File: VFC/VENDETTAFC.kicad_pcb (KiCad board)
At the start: 6 copper layers, 40 x 40 mm, 74 parts, among them IC1 MP1584EN-LF-Z, IC2 MP1584EN-LF-Z, J1 Conn_01x08_Socket, J2 Conn_01x06_Socket, J3 Conn_01x06_Socket, J4 Conn_01x03_Socket, P1 USB_C_Plug_USB2.0, SW1 SW_Push, U1 STM32F722RETx, U2 ICM-20948, U3 RT9701, U4 USBLC6-2P6, U5 W25Q128JVS, Y1 Crystal

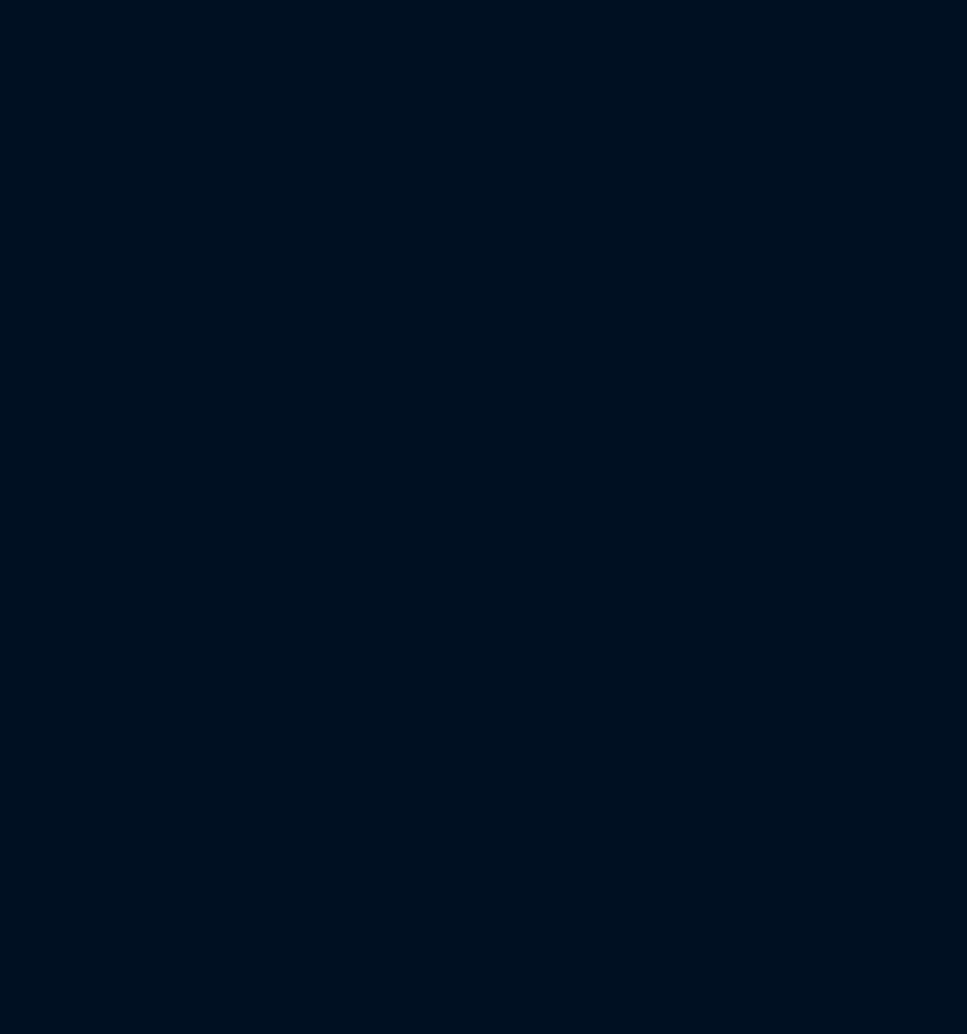
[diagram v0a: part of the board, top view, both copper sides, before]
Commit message: Updated VFC schematic
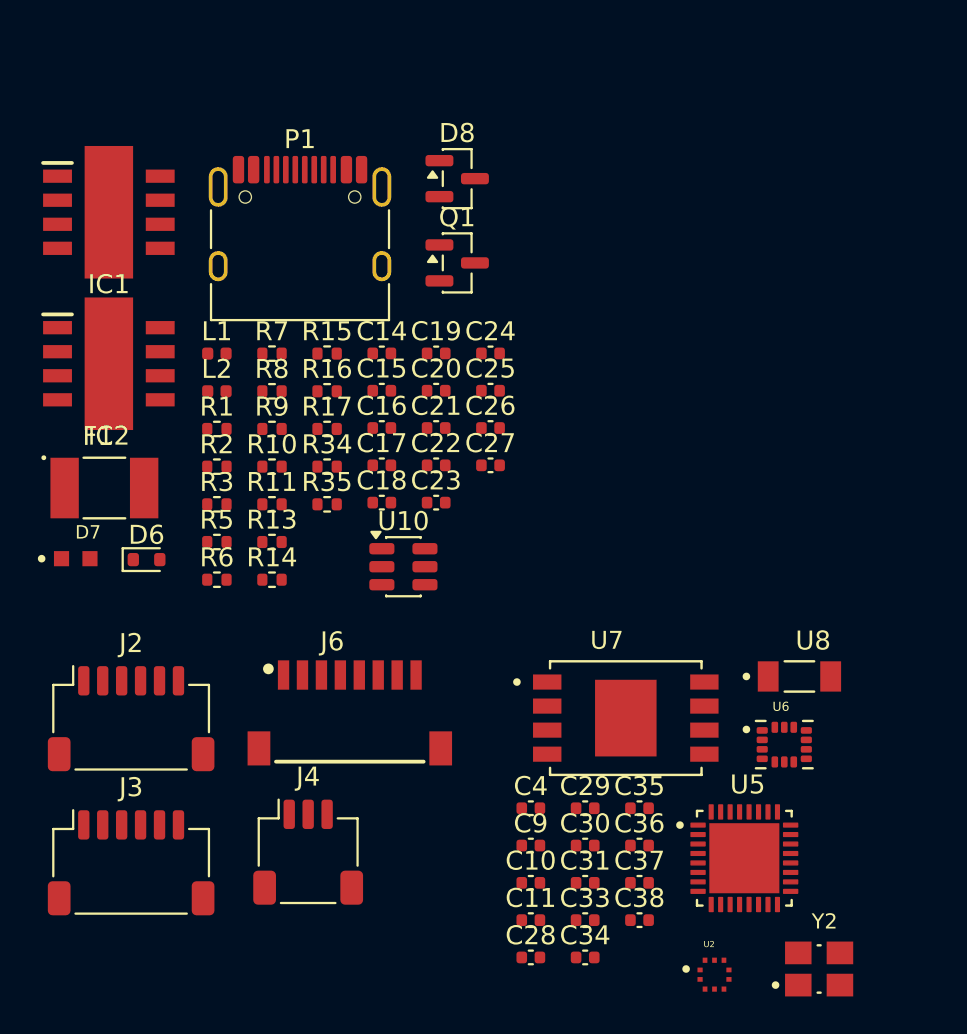
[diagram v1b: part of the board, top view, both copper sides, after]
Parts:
- added C10: 10nF, Capacitor_SMD:C_0402_1005Metric, F.Cu at (122.6, 145.5)
- added C11: 100nF, Capacitor_SMD:C_0402_1005Metric, F.Cu at (122.6, 147.5)
- added C14: 100nF, Capacitor_SMD:C_0402_1005Metric, F.Cu at (114.8, 117.6)
- added C15: 100nF, Capacitor_SMD:C_0402_1005Metric, F.Cu at (114.8, 119.5)
- added C16: 10uF, Capacitor_SMD:C_0402_1005Metric, F.Cu at (114.8, 121.5)
- added C17: 10uF, Capacitor_SMD:C_0402_1005Metric, F.Cu at (114.8, 123.5)
- added C18: 1uF, Capacitor_SMD:C_0402_1005Metric, F.Cu at (114.8, 125.4)
- added C19: 220pF, Capacitor_SMD:C_0402_1005Metric, F.Cu at (117.6, 117.6)
- added C20: 22uF, Capacitor_SMD:C_0402_1005Metric, F.Cu at (117.6, 119.5)
- added C21: 22uF, Capacitor_SMD:C_0402_1005Metric, F.Cu at (117.6, 121.5)
- added C22: 10uF, Capacitor_SMD:C_0402_1005Metric, F.Cu at (117.6, 123.5)
- added C23: 10uF, Capacitor_SMD:C_0402_1005Metric, F.Cu at (117.6, 125.4)
- added C24: 1uF, Capacitor_SMD:C_0402_1005Metric, F.Cu at (120.5, 117.6)
- added C25: 220pF, Capacitor_SMD:C_0402_1005Metric, F.Cu at (120.5, 119.5)
- added C26: 22uF, Capacitor_SMD:C_0402_1005Metric, F.Cu at (120.5, 121.5)
- added C27: 22uF, Capacitor_SMD:C_0402_1005Metric, F.Cu at (120.5, 123.5)
- added C28: 100nF, Capacitor_SMD:C_0402_1005Metric, F.Cu at (122.6, 149.5)
- added C29: 0.1uF, Capacitor_SMD:C_0402_1005Metric, F.Cu at (125.5, 141.6)
- added C30: 1pF, Capacitor_SMD:C_0402_1005Metric, F.Cu at (125.5, 143.5)
- added C31: 1pF, Capacitor_SMD:C_0402_1005Metric, F.Cu at (125.5, 145.5)
- added C33: 10nF, Capacitor_SMD:C_0402_1005Metric, F.Cu at (125.5, 147.5)
- added C34: 1uF, Capacitor_SMD:C_0402_1005Metric, F.Cu at (125.5, 149.5)
- added C35: 0.1uF, Capacitor_SMD:C_0402_1005Metric, F.Cu at (128.4, 141.6)
- added C36: 0.1uF, Capacitor_SMD:C_0402_1005Metric, F.Cu at (128.4, 143.5)
- added C37: 10uF, Capacitor_SMD:C_0402_1005Metric, F.Cu at (128.4, 145.5)
- added C38: 100nF, Capacitor_SMD:C_0402_1005Metric, F.Cu at (128.4, 147.5)
- added C4: 0.1uF, Capacitor_SMD:C_0402_1005Metric, F.Cu at (122.6, 141.6)
- added C9: 2.2uF, Capacitor_SMD:C_0402_1005Metric, F.Cu at (122.6, 143.5)
- added D6: LTVS16H5, Diode_SMD:D_SOD-523, F.Cu at (102.3, 128.4)
- added D7: KT-0603R, KT-0603R:LED_KT-0603R, F.Cu at (98.6, 128.4)
- added D8: BAT54C, Package_TO_SOT_SMD:SOT-23, F.Cu at (118.7, 108.3)
- added F1: MF-MSMF050-2, MF-MSMF050-2:FUSM4632X85, F.Cu at (100.1, 124.7)
- added IC1: MP1584EN-LF-Z, MP1584EN-LF-Z:SOIC127P600X170-9N, F.Cu at (100.3, 110.1)
- added IC2: MP1584EN-LF-Z, MP1584EN-LF-Z:SOIC127P600X170-9N, F.Cu at (100.3, 118.1)
- added J2: Conn_01x06_Socket, Connector_JST:JST_SH_SM06B-SRSS-TB_1x06-1MP_P1.00mm_Horizontal, F.Cu at (101.5, 136.8)
- added J3: Conn_01x06_Socket, Connector_JST:JST_SH_SM06B-SRSS-TB_1x06-1MP_P1.00mm_Horizontal, F.Cu at (101.5, 144.5)
- added J4: Conn_01x03_Socket, Connector_JST:JST_SH_SM03B-SRSS-TB_1x03-1MP_P1.00mm_Horizontal, F.Cu at (110.9, 143.9)
- added J6: SM08B-SRSS-TB_LF__SN_, SM08B-SRSS-TB_LF__SN_:JST_SM08B-SRSS-TB_LF__SN_, F.Cu at (113.1, 139.3)
- added L1: 10uH, Inductor_SMD:L_0402_1005Metric, F.Cu at (106.1, 117.6)
- added L2: 10uH, Inductor_SMD:L_0402_1005Metric, F.Cu at (106.1, 119.6)
- added P1: USB_C_Plug_USB2.0, Connector_USB:USB_C_Receptacle_HRO_TYPE-C-31-M-12, F.Cu at (110.4, 111.9)
- added Q1: AO3400A, Package_TO_SOT_SMD:SOT-23, F.Cu at (118.7, 112.8)
- added R1: 5k1, Resistor_SMD:R_0402_1005Metric, F.Cu at (106.1, 121.5)
- added R10: 20, Resistor_SMD:R_0402_1005Metric, F.Cu at (109.0, 123.5)
- added R11: 68K1, Resistor_SMD:R_0402_1005Metric, F.Cu at (109.0, 125.5)
- added R13: 200K, Resistor_SMD:R_0402_1005Metric, F.Cu at (109.0, 127.5)
- added R14: 20, Resistor_SMD:R_0402_1005Metric, F.Cu at (109.0, 129.5)
- added R15: 51K, Resistor_SMD:R_0402_1005Metric, F.Cu at (111.9, 117.6)
- added R16: 7K5, Resistor_SMD:R_0402_1005Metric, F.Cu at (111.9, 119.6)
- added R17: 41K2, Resistor_SMD:R_0402_1005Metric, F.Cu at (111.9, 121.5)
- added R2: 80, Resistor_SMD:R_0402_1005Metric, F.Cu at (106.1, 123.5)
- added R3: 80, Resistor_SMD:R_0402_1005Metric, F.Cu at (106.1, 125.5)
- added R34: 1K, Resistor_SMD:R_0402_1005Metric, F.Cu at (111.9, 123.5)
- added R35: 10K, Resistor_SMD:R_0402_1005Metric, F.Cu at (111.9, 125.5)
- added R5: 68K1, Resistor_SMD:R_0402_1005Metric, F.Cu at (106.1, 127.5)
- added R6: 200K, Resistor_SMD:R_0402_1005Metric, F.Cu at (106.1, 129.5)
- added R7: 51K, Resistor_SMD:R_0402_1005Metric, F.Cu at (109.0, 117.6)
- added R8: 41K2, Resistor_SMD:R_0402_1005Metric, F.Cu at (109.0, 119.6)
- added R9: 3K92, Resistor_SMD:R_0402_1005Metric, F.Cu at (109.0, 121.5)
- added U10: USBLC6-2SC6, Package_TO_SOT_SMD:SOT-23-6, F.Cu at (115.9, 128.8)
- added U2: BMP388, BMP388:XDCR_BMP388, F.Cu at (132.3, 150.4)
- added U5: ESP32-C3, ESP32-C3:QFN50P500X500X90-33N, F.Cu at (133.9, 144.2)
- added U6: ICM-42688-P, ICM-42688-P:PQFN50P300X250X97-14N, F.Cu at (136.0, 138.2)
- added U7: W25N04KVZEIR, W25N04KVZEIR:IC_W25N04KVZEIR, F.Cu at (127.7, 136.8)
- added U8: ~, crossair-ca-c03-antenna-1.snapshot.1:CA-C03, F.Cu at (136.8, 134.6)
- added Y2: C3E-40.000-10-1015-X-R, C3E-40.000-10-1015-X-R:XTAL_C3E-40.000-10-1015-X-R, F.Cu at (137.9, 150.1)
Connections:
- C1 pad 1: +3.3V -> ESP_EN
- C13 pad 1: +3.3V -> ESP_EN
- C2 pad 1: +3.3V -> ESP_EN
- C3 pad 1: +3.3V -> ESP_EN
- C5 pad 1: +3.3V -> ESP_EN
- C6 pad 1: +3.3V -> ESP_EN
- C7 pad 1: +3.3V -> ESP_EN
- D1 pad 2: +3.3V -> ESP_EN
- SW1 pad 1: +3.3V -> ESP_EN
- U1 pad 1: +3.3V -> ESP_EN
- U1 pad 13: +3.3V -> ESP_EN
- U1 pad 19: +3.3V -> ESP_EN
- U1 pad 32: +3.3V -> ESP_EN
- U1 pad 48: +3.3V -> ESP_EN
- U1 pad 64: +3.3V -> ESP_EN
- U3 pad 1: +3.3V -> ESP_EN
- U3 pad 5: +3.3V -> ESP_EN
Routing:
- net ESP_EN: track 0.00 -> 28.1 mm, vias 0 -> 10
- net +3.3V: track 36.7 -> 8.62 mm, vias 12 -> 2
- added copper zone on B.Cu, net ESP_EN
- added copper zone on In4.Cu, net ESP_EN
- removed copper zone on B.Cu, net +3.3V
- removed copper zone on In4.Cu, net +3.3V

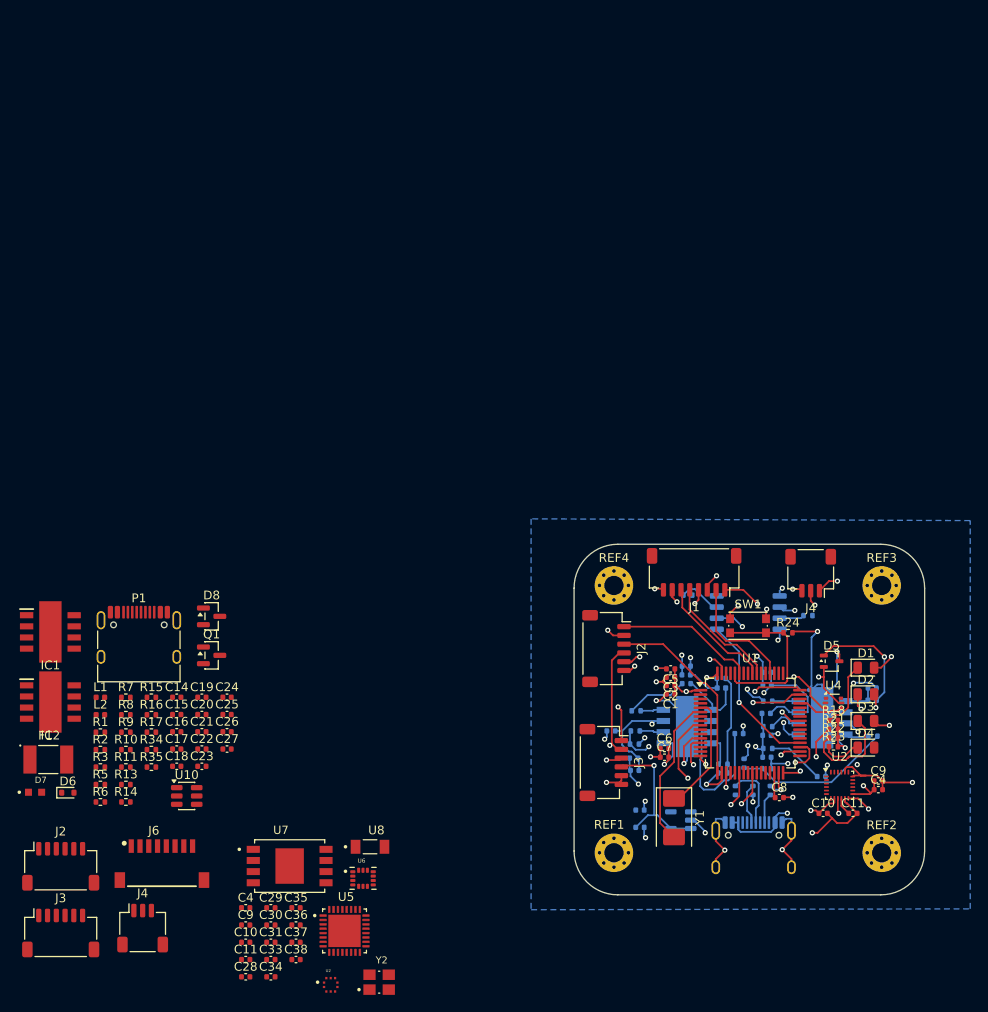
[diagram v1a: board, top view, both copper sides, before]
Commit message: VFC PCB components placements complete
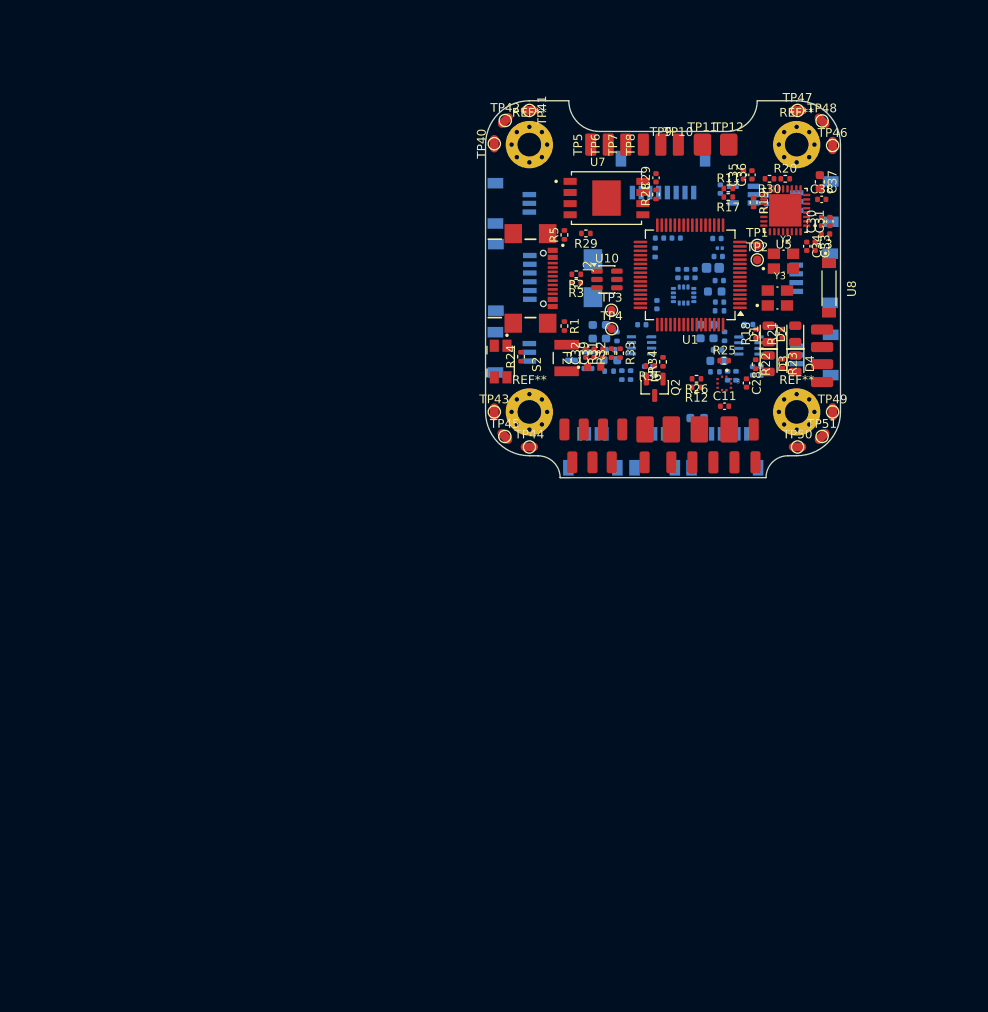
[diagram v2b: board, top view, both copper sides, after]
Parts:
- removed the C10 at (122.6, 145.5)
- removed the C10 at (188.5, 130.8)
- removed the C11 at (122.6, 147.5)
- removed the C11 at (191.9, 130.8)
- removed the C14 at (114.8, 117.6)
- removed the C14 at (172.9, 116.0)
- removed the C15 at (114.8, 119.5)
- removed the C15 at (194.1, 116.5)
- removed the C16 at (114.8, 121.5)
- removed the C16 at (167.0, 125.9)
- removed the C17 at (114.8, 123.5)
- removed the C17 at (164.3, 121.4)
- removed the C18 at (114.8, 125.4)
- removed the C18 at (166.9, 124.5)
- removed the C19 at (117.6, 117.6)
- removed the C19 at (178.9, 121.7)
- removed the C20 at (117.6, 119.5)
- removed the C20 at (172.9, 114.0)
- removed the C21 at (117.6, 121.5)
- removed the C21 at (172.9, 115.0)
- removed the C22 at (117.6, 123.5)
- removed the C22 at (182.0, 119.4)
- removed the C23 at (117.6, 125.4)
- removed the C23 at (182.1, 116.2)
- removed C24 (x2): 1uF, Capacitor_SMD:C_0402_1005Metric
- removed C25 (x2): 220pF, Capacitor_SMD:C_0402_1005Metric
- removed C26 (x2), C27 (x2): 22uF, Capacitor_SMD:C_0402_1005Metric
- removed the C4 at (194.8, 128.1)
- removed the C4 at (122.6, 141.6)
- removed the C9 at (194.8, 127.1)
- removed the C9 at (122.6, 143.5)
- removed D6: LTVS16H5, Diode_SMD:D_SOD-523
- removed F1: MF-MSMF050-2, MF-MSMF050-2:FUSM4632X85
- removed IC1 (x2), IC2 (x2): MP1584EN-LF-Z, MP1584EN-LF-Z:SOIC127P600X170-9N
- removed the J2 at (163.8, 112.0)
- removed the J2 at (101.5, 136.8)
- removed the J3 at (163.5, 125.0)
- removed the J3 at (101.5, 144.5)
- removed J4 (x2): Conn_01x03_Socket, Connector_JST:JST_SH_SM03B-SRSS-TB_1x03-1MP_P1.00mm_Horizontal
- removed the L1 at (106.1, 117.6)
- removed the L1 at (176.9, 116.5)
- removed the L2 at (106.1, 119.6)
- removed the L2 at (194.1, 117.9)
- removed P1 (x2): USB_C_Plug_USB2.0, Connector_USB:USB_C_Receptacle_HRO_TYPE-C-31-M-12
- removed Q1: AO3400A, Package_TO_SOT_SMD:SOT-23
- removed the R1 at (106.1, 121.5)
- removed the R1 at (182.5, 128.2)
- removed the R10 at (109.0, 123.5)
- removed the R10 at (167.2, 119.1)
- removed the R11 at (109.0, 125.5)
- removed the R11 at (182.2, 123.4)
- removed the R13 at (109.0, 127.5)
- removed the R13 at (182.2, 120.9)
- removed the R14 at (109.0, 129.5)
- removed the R14 at (182.2, 118.0)
- removed the R15 at (111.9, 117.6)
- removed the R15 at (194.2, 122.0)
- removed the R16 at (111.9, 119.6)
- removed the R16 at (179.5, 125.1)
- removed the R17 at (111.9, 121.5)
- removed the R17 at (182.1, 125.7)
- removed the R2 at (106.1, 123.5)
- removed the R2 at (180.5, 128.2)
- removed the R3 at (106.1, 125.5)
- removed the R3 at (178.5, 128.2)
- removed the R5 at (106.1, 127.5)
- removed the R5 at (167.0, 122.9)
- removed R6 (x2): 200K, Resistor_SMD:R_0402_1005Metric
- removed the R7 at (109.0, 117.6)
- removed the R7 at (177.1, 125.2)
- removed the R8 at (109.0, 119.6)
- removed the R8 at (176.9, 115.4)
- removed the R9 at (109.0, 121.5)
- removed the R9 at (177.1, 126.2)
- removed REF1, REF2, REF3, REF4: MountingHole_2.2mm_M2_Pad_Via, MountingHole:MountingHole_2.2mm_M2_Pad_Via
- removed SW1: SW_Push, Button_Switch_SMD:SW_Push_1P1T_NO_CK_KMR2
- removed the U2 at (190.4, 127.6)
- removed the U2 at (132.3, 150.4)
- removed the U5 at (133.9, 144.2)
- removed the U5 at (180.0, 107.9)
- removed Y1: Crystal, Crystal:Crystal_SMD_0603-2Pin_6.0x3.5mm
- added C10: 10nF, Capacitor_SMD:C_0402_1005Metric, B.Cu at (171.9, 69.2)
- added C11: 100nF, Capacitor_SMD:C_0402_1005Metric, F.Cu at (177.3, 84.3)
- added C14: 100nF, Capacitor_SMD:C_0402_1005Metric, B.Cu at (180.5, 80.3)
- added C15: 100nF, Capacitor_SMD:C_0402_1005Metric, B.Cu at (168.2, 80.3)
- added C16: 100nF, Capacitor_SMD:C_0402_1005Metric, B.Cu at (176.7, 70.0)
- added C17: 22uF, Capacitor_SMD:C_0603_1608Metric, B.Cu at (176.0, 75.8)
- added C18: 100uF, Capacitor_SMD:C_0603_1608Metric, B.Cu at (174.5, 75.8)
- added C19: 22uF, Capacitor_SMD:C_0603_1608Metric, B.Cu at (163.8, 75.8)
- added C20: 47uF, Capacitor_SMD:C_0603_1608Metric, B.Cu at (176.4, 79.2)
- added C21: 100uF, Capacitor_SMD:C_0603_1608Metric, B.Cu at (162.2, 75.8)
- added C22: 47uF, Capacitor_SMD:C_0603_1608Metric, B.Cu at (164.2, 79.1)
- added C23: 100nF, Capacitor_SMD:C_0402_1005Metric, B.Cu at (169.6, 72.8)
- added C32: 100nF, Capacitor_SMD:C_0402_1005Metric, F.Cu at (161.4, 78.3)
- added C39: 1uF, Capacitor_SMD:C_0402_1005Metric, F.Cu at (162.4, 78.3)
- added C4: 0.1uF, Capacitor_SMD:C_0402_1005Metric, B.Cu at (173.9, 69.2)
- added C40: 100uF, Capacitor_SMD:C_0603_1608Metric, B.Cu at (174.2, 85.7)
- added C41: 0.1uF, Capacitor_SMD:C_0402_1005Metric, B.Cu at (180.0, 75.0)
- added C42: 0.1uF, Capacitor_SMD:C_0402_1005Metric, B.Cu at (167.8, 75.0)
- added C9: 2.2uF, Capacitor_SMD:C_0402_1005Metric, B.Cu at (172.9, 69.2)
- added F2: MICROASMD010F-2, MICROASMD010F-2:FUSE_MICROASMD010F_LTF, F.Cu at (159.2, 78.8)
- added FL1: 120, BLM03EB500SZ1D:BEADC0603X33N, B.Cu at (176.7, 66.3)
- added J10: SM04B-SRSS-TB_LF__SN_, SM04B-SRSS-TB_LF__SN_:JST_SM04B-SRSS-TB_LF__SN_, B.Cu at (185.4, 69.8)
- added J11: SM04B-SRSS-TB_LF__SN_, SM04B-SRSS-TB_LF__SN_:JST_SM04B-SRSS-TB_LF__SN_, B.Cu at (162.2, 87.5)
- added J12: SM03B-SRSS-TB_LF__SN_, SM03B-SRSS-TB_LF__SN_:JST_SM03B-SRSS-TB_LF__SN_, B.Cu at (169.3, 87.5)
- added J2: USB4940-00-A_REVA, USB4940-00-A_REVA:GCT_USB4940-00-A_REVA, F.Cu at (156.6, 69.8)
- added J3: SM03B-SRSS-TB_LF__SN_, SM03B-SRSS-TB_LF__SN_:JST_SM03B-SRSS-TB_LF__SN_, B.Cu at (155.0, 61.2)
- added J5: SM03B-SRSS-TB_LF__SN_, SM03B-SRSS-TB_LF__SN_:JST_SM03B-SRSS-TB_LF__SN_, B.Cu at (155.0, 78.2)
- added J7: SM03B-SRSS-TB_LF__SN_, SM03B-SRSS-TB_LF__SN_:JST_SM03B-SRSS-TB_LF__SN_, B.Cu at (185.5, 61.0)
- added J8: SM03B-SRSS-TB_LF__SN_, SM03B-SRSS-TB_LF__SN_:JST_SM03B-SRSS-TB_LF__SN_, B.Cu at (185.5, 78.5)
- added J9: SM06B-SRSS-TB_LF__SN_, SM06B-SRSS-TB_LF__SN_:JST_SM06B-SRSS-TB_LF__SN_, B.Cu at (155.1, 69.7)
- added L1: 10uH, Inductor_SMD:L_0402_1005Metric, B.Cu at (176.5, 77.9)
- added L2: 10uH, Inductor_SMD:L_0402_1005Metric, B.Cu at (164.2, 77.9)
- added L3: 2nH, Inductor_SMD:L_0402_1005Metric, F.Cu at (188.8, 64.7)
- added Q2: AO3400A, Package_TO_SOT_SMD:SOT-23, F.Cu at (169.3, 82.2)
- added R1: 5k1, Resistor_SMD:R_0402_1005Metric, F.Cu at (159.0, 75.2)
- added R10: 20, Resistor_SMD:R_0402_1005Metric, B.Cu at (181.4, 80.3)
- added R11: 18K, Resistor_SMD:R_0402_1005Metric, F.Cu at (177.7, 59.5)
- added R12: 10K, Resistor_SMD:R_0402_1005Metric, F.Cu at (174.1, 82.2)
- added R13: 20, Resistor_SMD:R_0402_1005Metric, B.Cu at (169.1, 80.3)
- added R14: 51K, Resistor_SMD:R_0402_1005Metric, B.Cu at (166.6, 80.8)
- added R15: 7K5, Resistor_SMD:R_0402_1005Metric, B.Cu at (165.6, 80.8)
- added R16: 41K2, Resistor_SMD:R_0402_1005Metric, B.Cu at (164.1, 80.3)
- added R17: 2K, Resistor_SMD:R_0402_1005Metric, F.Cu at (177.7, 60.5)
- added R2: 80, Resistor_SMD:R_0402_1005Metric, F.Cu at (160.3, 69.3)
- added R25: 2.2K, Resistor_SMD:R_0402_1005Metric, F.Cu at (177.2, 79.2)
- added R26: 2.2K, Resistor_SMD:R_0402_1005Metric, F.Cu at (174.1, 81.2)
- added R27: 4.7K, Resistor_SMD:R_0402_1005Metric, B.Cu at (169.3, 66.8)
- added R28: 4.7K, Resistor_SMD:R_0402_1005Metric, F.Cu at (169.4, 60.2)
- added R29: 4.7K, Resistor_SMD:R_0402_1005Metric, F.Cu at (161.4, 64.6)
- added R3: 80, Resistor_SMD:R_0402_1005Metric, F.Cu at (160.3, 70.2)
- added R30: 10K, Resistor_SMD:R_0402_1005Metric, F.Cu at (182.4, 58.4)
- added R31: 220, Resistor_SMD:R_0402_1005Metric, F.Cu at (163.4, 78.3)
- added R32: 5.1K, Resistor_SMD:R_0402_1005Metric, F.Cu at (164.4, 78.3)
- added R33: 10K, Resistor_SMD:R_0402_1005Metric, F.Cu at (165.3, 78.3)
- added R36: 1M, Resistor_SMD:R_0402_1005Metric, B.Cu at (177.3, 76.4)
- added R37: 1M, Resistor_SMD:R_0402_1005Metric, B.Cu at (165.0, 76.4)
- added R4: 10K, Resistor_SMD:R_0402_1005Metric, B.Cu at (176.7, 73.5)
- added R5: 5k1, Resistor_SMD:R_0402_1005Metric, F.Cu at (159.0, 64.8)
- added R7: 51K, Resistor_SMD:R_0402_1005Metric, B.Cu at (178.6, 80.9)
- added R8: 41K2, Resistor_SMD:R_0402_1005Metric, B.Cu at (176.2, 80.4)
- added R9: 3K92, Resistor_SMD:R_0402_1005Metric, B.Cu at (177.6, 80.9)
- added REF**: MountingHole_2.7mm_M2.5_Pad_Via, MountingHole:MountingHole_2.7mm_M2.5_Pad_Via, F.Cu at (185.5, 54.5)
- added REF**: MountingHole_2.7mm_M2.5_Pad_Via, MountingHole:MountingHole_2.7mm_M2.5_Pad_Via, F.Cu at (155.0, 54.5)
- added REF**: MountingHole_2.7mm_M2.5_Pad_Via, MountingHole:MountingHole_2.7mm_M2.5_Pad_Via, F.Cu at (155.0, 85.0)
- added REF**: MountingHole_2.7mm_M2.5_Pad_Via, MountingHole:MountingHole_2.7mm_M2.5_Pad_Via, F.Cu at (185.5, 85.0)
- added S2: EVQ-P7A01P, EVQ-P7A01P:SW_EVQ-P7A01P, F.Cu at (151.7, 79.2)
- added TP1: TestPoint, TestPoint:TestPoint_Pad_D1.0mm, F.Cu at (181.0, 66.0)
- added TP10: TestPoint, TestPoint:TestPoint_Pad_D1.0mm, F.Cu at (172.0, 54.5)
- added TP11: TestPoint, TestPoint:TestPoint_Pad_D2.0mm, F.Cu at (174.8, 54.5)
- added TP12: TestPoint, TestPoint:TestPoint_Pad_D2.0mm, F.Cu at (177.8, 54.5)
- added TP13: TestPoint, TestPoint:TestPoint_Pad_1.0x1.0mm, F.Cu at (180.8, 90.8)
- added TP14: TestPoint, TestPoint:TestPoint_Pad_1.0x1.0mm, F.Cu at (178.4, 90.8)
- added TP15: TestPoint, TestPoint:TestPoint_Pad_1.0x1.0mm, F.Cu at (176.0, 90.8)
- added TP16: TestPoint, TestPoint:TestPoint_Pad_1.0x1.0mm, F.Cu at (173.6, 90.8)
- added TP17: TestPoint, TestPoint:TestPoint_Pad_2.0x2.0mm, F.Cu at (177.8, 87.0)
- added TP18: TestPoint, TestPoint:TestPoint_Pad_1.0x1.0mm, F.Cu at (174.4, 87.0)
- added TP19: TestPoint, TestPoint:TestPoint_Pad_1.0x1.0mm, F.Cu at (180.6, 87.0)
- added TP2: TestPoint, TestPoint:TestPoint_Pad_D1.0mm, F.Cu at (181.0, 67.7)
- added TP23: TestPoint, TestPoint:TestPoint_Pad_1.0x1.0mm, F.Cu at (159.0, 87.0)
- added TP24: TestPoint, TestPoint:TestPoint_Pad_1.0x1.0mm, F.Cu at (161.2, 87.0)
- added TP25: TestPoint, TestPoint:TestPoint_Pad_1.0x1.0mm, F.Cu at (163.4, 87.0)
- added TP26: TestPoint, TestPoint:TestPoint_Pad_1.0x1.0mm, F.Cu at (165.6, 87.0)
- added TP29: TestPoint, TestPoint:TestPoint_Pad_1.0x1.0mm, F.Cu at (188.4, 81.6)
- added TP3: TestPoint, TestPoint:TestPoint_Pad_D1.0mm, F.Cu at (164.4, 73.4)
- added TP30: TestPoint, TestPoint:TestPoint_Pad_1.0x1.0mm, F.Cu at (188.4, 79.5)
- added TP31: TestPoint, TestPoint:TestPoint_Pad_2.0x2.0mm, F.Cu at (188.4, 77.6)
- added TP32: TestPoint, TestPoint:TestPoint_Pad_1.0x1.0mm, F.Cu at (188.4, 75.6)
- added TP33: TestPoint, TestPoint:TestPoint_Pad_1.0x1.0mm, F.Cu at (164.4, 90.8)
- added TP34: TestPoint, TestPoint:TestPoint_Pad_1.0x1.0mm, F.Cu at (162.2, 90.8)
- added TP35: TestPoint, TestPoint:TestPoint_Pad_2.0x2.0mm, F.Cu at (168.2, 87.0)
- added TP36: TestPoint, TestPoint:TestPoint_Pad_1.0x1.0mm, F.Cu at (159.9, 90.8)
- added TP37: TestPoint, TestPoint:TestPoint_Pad_2.0x2.0mm, F.Cu at (171.2, 87.0)
- added TP38: TestPoint, TestPoint:TestPoint_Pad_1.0x1.0mm, F.Cu at (171.2, 90.8)
- added TP39: TestPoint, TestPoint:TestPoint_Pad_1.0x1.0mm, F.Cu at (168.2, 90.8)
- added TP4: TestPoint, TestPoint:TestPoint_Pad_D1.0mm, F.Cu at (164.4, 75.5)
- added TP40: TestPoint, TestPoint:TestPoint_Pad_D1.0mm, F.Cu at (151.0, 54.4)
- added TP41: TestPoint, TestPoint:TestPoint_Pad_D1.0mm, F.Cu at (155.0, 50.6)
- added TP42: TestPoint, TestPoint:TestPoint_Pad_D1.0mm, F.Cu at (152.2, 51.8)
- added TP43: TestPoint, TestPoint:TestPoint_Pad_D1.0mm, F.Cu at (151.0, 85.0)
- added TP44: TestPoint, TestPoint:TestPoint_Pad_D1.0mm, F.Cu at (155.0, 89.0)
- added TP45: TestPoint, TestPoint:TestPoint_Pad_D1.0mm, F.Cu at (152.2, 87.8)
- added TP46: TestPoint, TestPoint:TestPoint_Pad_D1.0mm, F.Cu at (189.6, 54.6)
- added TP47: TestPoint, TestPoint:TestPoint_Pad_D1.0mm, F.Cu at (185.6, 50.6)
- added TP48: TestPoint, TestPoint:TestPoint_Pad_D1.0mm, F.Cu at (188.4, 51.8)
- added TP49: TestPoint, TestPoint:TestPoint_Pad_D1.0mm, F.Cu at (189.6, 85.0)
- added TP5: TestPoint, TestPoint:TestPoint_Pad_D1.0mm, F.Cu at (162.0, 54.5)
- added TP50: TestPoint, TestPoint:TestPoint_Pad_D1.0mm, F.Cu at (185.6, 89.0)
- added TP51: TestPoint, TestPoint:TestPoint_Pad_D1.0mm, F.Cu at (188.4, 87.8)
- added TP6: TestPoint, TestPoint:TestPoint_Pad_D1.0mm, F.Cu at (164.0, 54.5)
- added TP7: TestPoint, TestPoint:TestPoint_Pad_D1.0mm, F.Cu at (166.0, 54.5)
- added TP8: TestPoint, TestPoint:TestPoint_Pad_D1.0mm, F.Cu at (168.0, 54.5)
- added TP9: TestPoint, TestPoint:TestPoint_Pad_D1.0mm, F.Cu at (170.0, 54.5)
- added U2: BMP388, BMP388:XDCR_BMP388, F.Cu at (177.2, 81.8)
- added U5: ESP32-C3, ESP32-C3:QFN50P500X500X90-33N, F.Cu at (184.2, 62.0)
- added U9: ~, MP9943GQ-Z:QFN-8_MP9943_MNP, B.Cu at (167.8, 77.4)
- added Y3: C3E-8.000-18-3030-X-R, C3E-8.000-18-3030-X-R:XTAL_C3E-8.000-18-3030-X-R, F.Cu at (183.3, 72.0)
- C1, C2, C3, C6, D8, J6, U6: moved to B.Cu
- C12, C13: value 1nF -> 1uF
- C37: footprint Capacitor_SMD:C_0402_1005Metric -> Capacitor_SMD:C_0603_1608Metric
- C5: footprint Capacitor_SMD:C_0402_1005Metric -> Capacitor_SMD:C_0603_1608Metric; moved to B.Cu
- C7: footprint Capacitor_SMD:C_0402_1005Metric -> Capacitor_Tantalum_SMD:CP_EIA-1608-08_AVX-J; moved to B.Cu
- C8: value 2.2uf -> 2.2uF; moved to B.Cu
- D5: value BAT54CW -> SMBJ30A; footprint Package_TO_SOT_SMD:SOT-323_SC-70 -> SMBJ30A:DIOM4336X265N; moved to B.Cu
- J1: value Conn_01x08_Socket -> SM06B-SRSS-TB_LF__SN_; footprint Connector_JST:JST_SH_SM08B-SRSS-TB_1x08-1MP_P1.00mm_Horizontal -> SM06B-SRSS-TB_LF__SN_:JST_SM06B-SRSS-TB_LF__SN_; moved to B.Cu
- R19, R20: moved to F.Cu
- U3: value RT9701 -> AP2112K-3.3TRG1; footprint Package_TO_SOT_SMD:SOT-23-5 -> AP2112K-3.3TRG1:SOT95P285X140-5N
- U4: value USBLC6-2P6 -> ~; footprint Package_TO_SOT_SMD:SOT-666 -> MP9943GQ-Z:QFN-8_MP9943_MNP; moved to B.Cu
- moved C38 105.5 mm to (188.4, 60.8)
- moved C37 105.4 mm to (188.1, 58.8), turned to -90 degrees
- moved C31 104.1 mm to (189.3, 63.3), turned to 90 degrees
- moved C34 103.4 mm to (186.7, 66.1), turned to -90 degrees
- moved C33 102.4 mm to (187.6, 66.1), turned to -90 degrees
- moved C30 101.9 mm to (188.3, 63.3), turned to 90 degrees
- moved J6 101.7 mm to (170.2, 55.2)
- moved C36 100.2 mm to (180.4, 58.0), turned to 90 degrees
- moved C35 98.0 mm to (179.4, 58.0), turned to 90 degrees
- moved Y2 94.3 mm to (184.0, 67.8)
- moved C29 94.2 mm to (169.4, 58.3), turned to 90 degrees
- moved C28 88.6 mm to (179.8, 81.7), turned to -90 degrees
- moved U7 84.4 mm to (163.8, 60.6)
- moved U8 82.5 mm to (189.2, 70.9), turned to -90 degrees
- moved D7 80.1 mm to (162.4, 79.9)
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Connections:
- C1 pad 1: ESP_EN -> +3.3V
- C13 pad 1: ESP_EN -> +3.3V
- C2 pad 1: ESP_EN -> +3.3V
- C28 pad 1: ESP_EN -> +3.3V
- C29 pad 1: ESP_EN -> +3.3V
- C3 pad 1: ESP_EN -> +3.3V
- C33 pad 1: ESP_EN -> +3.3V
- C34 pad 1: ESP_EN -> +3.3V
- C35 pad 1: ESP_EN -> +3.3V
- C36 pad 1: ESP_EN -> +3.3V
- C37 pad 1: ESP_EN -> +3.3V
- C38 pad 1: ESP_EN -> +3.3V
- C5 pad 1: ESP_EN -> +3.3V
- C6 pad 1: ESP_EN -> +3.3V
- C7 pad 1: ESP_EN -> +3.3V
- D1 pad 2: ESP_EN -> +3.3V
- D4 pad 2: /LED0 -> U_LED
- J1 pad 1: /ADC_CUR -> UART4_RX
- J1 pad 2: /UART3_RX -> GND
- J1 pad 3: /MOTOR4 -> UART3_RX
- J1 pad 4: /MOTOR3 -> UART3_TX
- J1 pad 5: /MOTOR2 -> GND
- J1 pad 6: /MOTOR1 -> +9V
- J6 pad 1: M3 -> M4
- J6 pad 2: M2 -> M3
- J6 pad 3: M1 -> M2
- J6 pad 4: ADC_CUR -> M1
- R19 pad 2: Net-(U5-~{WP}/IO_{2}) -> ESP_CS
- R20 pad 1: +3.3V -> Net-(U5-GPIO8)
- R20 pad 2: Net-(U5-~{HOLD}/~{RESET}/IO_{3}) -> +3.3V
- U1 pad 1: ESP_EN -> +3.3V
- U1 pad 11: /ADC_VBAT -> ESP_CS
- U1 pad 13: ESP_EN -> Net-(U1-VDDA)
- U1 pad 14: /UART4_TX -> UART5_TX
- U1 pad 15: /UART4_RX -> UART5_RX
- U1 pad 16: /UART2_TX -> M4
- U1 pad 17: /UART2_RX -> M3
- U1 pad 19: ESP_EN -> +3.3V
- U1 pad 2: unconnected-(U1-PC13-Pad2) -> ADC_CUR
- U1 pad 20: /GYRO_CS -> LED3
- U1 pad 21: /SPI1_SCK -> ESP_SCK
- U1 pad 22: /SPI1_SDO -> ESP_MISO
- U1 pad 23: /SPI1_SDI -> ESP_MOSI
- U1 pad 24: unconnected-(U1-PC4-Pad24) -> ESC_RX
- U1 pad 25: /GYRO_INT -> M2
- U1 pad 26: unconnected-(U1-PB1-Pad26) -> M1
- U1 pad 28: /I2C_SCL -> LED1
- U1 pad 29: /I2C_SDA -> U_LED
- U1 pad 3: unconnected-(U1-PC14-Pad3) -> LED4
- U1 pad 32: ESP_EN -> +3.3V
- U1 pad 33: unconnected-(U1-PB12-Pad33) -> FLS_CS
- U1 pad 34: /SPI2_SCK -> FLS_SCK
- U1 pad 35: /SPI2_SDO -> FLS_MISO
- U1 pad 36: /SPI2_SDI -> FLS_MOSI
- U1 pad 37: unconnected-(U1-PC6-Pad37) -> UART7_TX
- U1 pad 38: /MOTOR3 -> UART7_RX
- U1 pad 39: /MOTOR4 -> LED2
- U1 pad 4: /BUZZER -> BUZZ
- U1 pad 40: unconnected-(U1-PC9-Pad40) -> GPS_SDA
- U1 pad 41: /FLASH_CS -> GPS_SCL
- U1 pad 42: /UART5_TX -> UART6_TX
- U1 pad 43: /UART5_RX -> UART6_RX
- U1 pad 44: /USB_D+ -> USB_D-
- U1 pad 45: /USB_D- -> USB_D+
- U1 pad 46: /LED0 -> SWDIO
- U1 pad 48: ESP_EN -> +3.3V
- U1 pad 49: unconnected-(U1-PA14-Pad49) -> SWCLK
- U1 pad 50: unconnected-(U1-PA15-Pad50) -> USB_VBUS_SENSE
- U1 pad 51: /UART3_TX -> UART4_TX
- U1 pad 52: /UART3_RX -> UART4_RX
- U1 pad 53: unconnected-(U1-PC12-Pad53) -> UART3_TX
- U1 pad 54: unconnected-(U1-PD2-Pad54) -> UART3_RX
- U1 pad 55: /MOTOR2 -> IMU_SCK
- U1 pad 56: /MOTOR1 -> IMU_MISO
- U1 pad 57: unconnected-(U1-PB5-Pad57) -> IMU_MOSI
- U1 pad 58: /UART1_TX -> BAR_SCL
- U1 pad 59: /UART1_RX -> BAR_SDA
- U1 pad 61: unconnected-(U1-PB8-Pad61) -> IMU_INT
- U1 pad 62: unconnected-(U1-PB9-Pad62) -> IMU_CS
- U1 pad 64: ESP_EN -> +3.3V
- U1 pad 7: unconnected-(U1-NRST-Pad7) -> Net-(U1-NRST)
- U1 pad 9: /ADC_CUR -> ADC_VBAT
- U3 pad 1: ESP_EN -> +5V
- U3 pad 4: +5V -> (no net)
- U3 pad 5: ESP_EN -> +3.3V
- U4 pad 1: /USB_CON_D+ -> Net-(U4-FB)
- U4 pad 2: GND -> Net-(U4-PG)
- U4 pad 3: /USB_CON_D- -> Net-(U4-EN/SYNC)
- U4 pad 4: /USB_D- -> Net-(U4-BST)
- U4 pad 5: VBUS -> GND
- U4 pad 6: /USB_D+ -> Net-(U4-SW)
- U6 pad 5: ESP_EN -> +3.3V
- U6 pad 8: ESP_EN -> +3.3V
- U7 pad 8: ESP_EN -> +3.3V
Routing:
- net GND: track 158.3 -> 0.00 mm, vias 36 -> 0
- net +9V: track 59.9 -> 0.00 mm, vias 4 -> 0
- net +VLIPO: track 57.3 -> 0.00 mm, vias 3 -> 0
- net +5V: track 47.6 -> 0.00 mm, vias 2 -> 0
- net /VIDEO: track 37.5 -> 0.00 mm, vias 2 -> 0
- net +5VBAT: track 36.4 -> 0.00 mm, vias 3 -> 0
- net /ADC_CUR: track 35.6 -> 0.00 mm, vias 2 -> 0
- net VBUS: track 32.7 -> 0.00 mm, vias 2 -> 0
- net ESP_EN: track 28.1 -> 0.00 mm, vias 10 -> 0
- net /UART2_TX: track 26.6 -> 0.00 mm, vias 2 -> 0
- net /SPI2_SDO: track 23.6 -> 0.00 mm, vias 2 -> 0
- net /USB_CON_D-: track 22.6 -> 0.00 mm, vias 2 -> 0
- net /SPI2_SCK: track 22.1 -> 0.00 mm, vias 2 -> 0
- net /GYRO_INT: track 22.0 -> 0.00 mm, vias 2 -> 0
- net /UART2_RX: track 21.9 -> 0.00 mm
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- removed copper zone on B.Cu, net ESP_EN
- removed copper zone on In4.Cu, net ESP_EN
- removed copper zone on In1.Cu, net GND
- removed copper zone on In4.Cu, net GND
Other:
- board size 40 x 40 mm -> 40.5 x 43 mm
